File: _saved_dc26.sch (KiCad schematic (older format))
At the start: 60 parts, among them J1 CONN_01X10, J2 CONN_01X10, J3 CONN_01X10

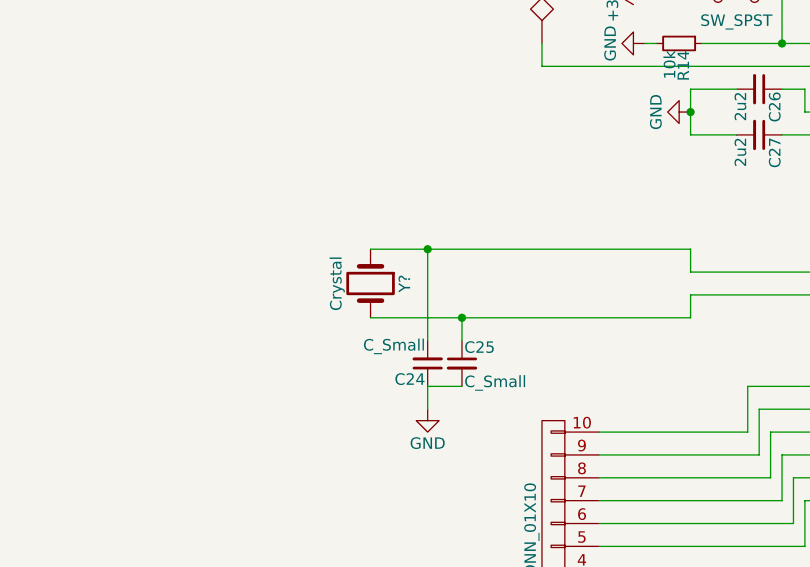
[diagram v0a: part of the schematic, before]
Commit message: zone movement + routing of all circuits
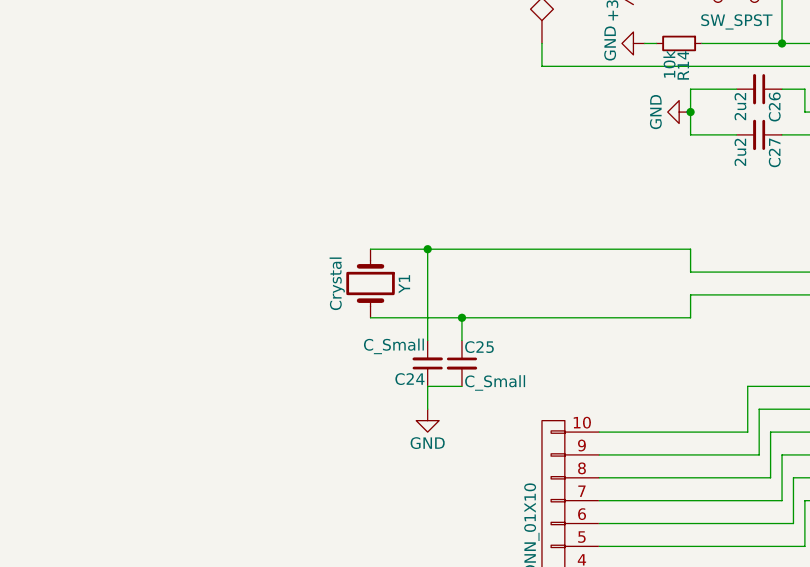
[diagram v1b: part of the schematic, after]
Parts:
- gave numbers to parts that had none: 1
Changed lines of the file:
@@
 $EndComp
 $Comp
-L VCC #PWR01
+L VCC #PWR14
 U 1 1 5AD008FD
 P -5650 -6600
-F 0 "#PWR01" H -5650 -6750 50  0001 C CNN
+F 0 "#PWR14" H -5650 -6750 50  0001 C CNN
 F 1 "VCC" H -5650 -6450 50  0000 C CNN
 F 2 "" H -5650 -6600 50  0001 C CNN
@@
 $EndComp
 $Comp
-L GND #PWR02
+L GND #PWR18
 U 1 1 5AD27FBE
 P -3800 -6700
-F 0 "#PWR02" H -3800 -6950 50  0001 C CNN
+F 0 "#PWR18" H -3800 -6950 50  0001 C CNN
 F 1 "GND" H -3800 -6850 50  0000 C CNN
 F 2 "" H -3800 -6700 50  0001 C CNN
@@
 $EndComp
 $Comp
-L GND #PWR03
+L GND #PWR2
 U 1 1 5AD5BD83
 P -12550 1050
-F 0 "#PWR03" H -12550 800 50  0001 C CNN
+F 0 "#PWR2" H -12550 800 50  0001 C CNN
 F 1 "GND" H -12550 900 50  0000 C CNN
 F 2 "" H -12550 1050 50  0001 C CNN
@@
 $EndComp
 $Comp
-L VCC #PWR04
+L VCC #PWR6
 U 1 1 5AD5C4E4
 P -12300 1050
-F 0 "#PWR04" H -12300 900 50  0001 C CNN
+F 0 "#PWR6" H -12300 900 50  0001 C CNN
 F 1 "VCC" H -12300 1200 50  0000 C CNN
 F 2 "" H -12300 1050 50  0001 C CNN
@@
 $EndComp
 $Comp
-L GND #PWR05
+L GND #PWR20
 U 1 1 5AD6E593
 P -2500 -5100
-F 0 "#PWR05" H -2500 -5350 50  0001 C CNN
+F 0 "#PWR20" H -2500 -5350 50  0001 C CNN
 F 1 "GND" H -2500 -5250 50  0000 C CNN
 F 2 "" H -2500 -5100 50  0001 C CNN
@@
 $EndComp
 $Comp
-L GND #PWR06
+L GND #PWR21
 U 1 1 5AD6F999
 P -2500 -3550
-F 0 "#PWR06" H -2500 -3800 50  0001 C CNN
+F 0 "#PWR21" H -2500 -3800 50  0001 C CNN
 F 1 "GND" H -2500 -3700 50  0000 C CNN
 F 2 "" H -2500 -3550 50  0001 C CNN
@@
 $EndComp
 $Comp
-L GND #PWR07
+L GND #PWR19
 U 1 1 5AD77A72
 P -3600 -800
-F 0 "#PWR07" H -3600 -1050 50  0001 C CNN
+F 0 "#PWR19" H -3600 -1050 50  0001 C CNN
 F 1 "GND" H -3600 -950 50  0000 C CNN
 F 2 "" H -3600 -800 50  0001 C CNN
@@
 $EndComp
 $Comp
-L VCC #PWR08
+L VCC #PWR11
 U 1 1 5AD946E2
 P -7100 12550
-F 0 "#PWR08" H -7100 12400 50  0001 C CNN
+F 0 "#PWR11" H -7100 12400 50  0001 C CNN
 F 1 "VCC" H -7100 12700 50  0000 C CNN
 F 2 "" H -7100 12550 50  0001 C CNN
@@
 $EndComp
 $Comp
-L GND #PWR09
+L GND #PWR10
 U 1 1 5AD98D43
 P -7100 12200
-F 0 "#PWR09" H -7100 11950 50  0001 C CNN
+F 0 "#PWR10" H -7100 11950 50  0001 C CNN
 F 1 "GND" H -7100 12050 50  0000 C CNN
 F 2 "" H -7100 12200 50  0001 C CNN
@@
 $EndComp
 $Comp
-L GND #PWR010
+L GND #PWR17
 U 1 1 5ADAF5CF
 P -3950 10600
-F 0 "#PWR010" H -3950 10350 50  0001 C CNN
+F 0 "#PWR17" H -3950 10350 50  0001 C CNN
 F 1 "GND" H -3950 10450 50  0000 C CNN
 F 2 "" H -3950 10600 50  0001 C CNN
@@
 $EndComp
 $Comp
-L GND #PWR011
+L GND #PWR15
 U 1 1 5ADAFD4C
 P -4000 9500
-F 0 "#PWR011" H -4000 9250 50  0001 C CNN
+F 0 "#PWR15" H -4000 9250 50  0001 C CNN
 F 1 "GND" H -4000 9350 50  0000 C CNN
 F 2 "" H -4000 9500 50  0001 C CNN
@@
 $EndComp
 $Comp
-L GND #PWR012
+L GND #PWR16
 U 1 1 5ADB04C2
 P -4000 12400
-F 0 "#PWR012" H -4000 12150 50  0001 C CNN
+F 0 "#PWR16" H -4000 12150 50  0001 C CNN
 F 1 "GND" H -4000 12250 50  0000 C CNN
 F 2 "" H -4000 12400 50  0001 C CNN
@@
 $EndComp
 $Comp
-L GND #PWR013
+L GND #PWR12
 U 1 1 5B04F2A2
 P -7000 8800
-F 0 "#PWR013" H -7000 8550 50  0001 C CNN
+F 0 "#PWR12" H -7000 8550 50  0001 C CNN
 F 1 "GND" H -7000 8650 50  0000 C CNN
 F 2 "" H -7000 8800 50  0001 C CNN
@@
 $EndComp
 $Comp
-L GND #PWR014
+L GND #PWR1
 U 1 1 5B0E23AB
 P -13400 6550
-F 0 "#PWR014" H -13400 6300 50  0001 C CNN
+F 0 "#PWR1" H -13400 6300 50  0001 C CNN
 F 1 "GND" H -13400 6400 50  0000 C CNN
 F 2 "" H -13400 6550 50  0001 C CNN
@@
 $EndComp
 $Comp
-L +3.3V #PWR016
+L +3.3V #PWR9
 U 1 1 5B0D3E01
 P -7200 2050
-F 0 "#PWR016" H -7200 1900 50  0001 C CNN
+F 0 "#PWR9" H -7200 1900 50  0001 C CNN
 F 1 "+3.3V" H -7200 2190 50  0000 C CNN
 F 2 "" H -7200 2050 50  0001 C CNN
@@
 $EndComp
 $Comp
-L GND #PWR017
+L GND #PWR7
 U 1 1 5B0F137D
 P -12250 5250
-F 0 "#PWR017" H -12250 5000 50  0001 C CNN
+F 0 "#PWR7" H -12250 5000 50  0001 C CNN
 F 1 "GND" H -12250 5100 50  0000 C CNN
 F 2 "" H -12250 5250 50  0001 C CNN
@@
 $EndComp
 $Comp
-L GND #PWR018
+L GND #PWR13
 U 1 1 5B0F6A9C
 P -6200 3750
-F 0 "#PWR018" H -6200 3500 50  0001 C CNN
+F 0 "#PWR13" H -6200 3500 50  0001 C CNN
 F 1 "GND" H -6200 3600 50  0000 C CNN
 F 2 "" H -6200 3750 50  0001 C CNN
@@
 $EndComp
 $Comp
-L +3.3V #PWR019
+L +3.3V #PWR8
 U 1 1 5B11C638
 P -11750 3950
-F 0 "#PWR019" H -11750 3800 50  0001 C CNN
+F 0 "#PWR8" H -11750 3800 50  0001 C CNN
 F 1 "+3.3V" H -11750 4090 50  0000 C CNN
 F 2 "" H -11750 3950 50  0001 C CNN
@@
 $EndComp
 $Comp
-L GND #PWR020
+L GND #PWR5
 U 1 1 5B12677B
 P -12400 4350
-F 0 "#PWR020" H -12400 4100 50  0001 C CNN
+F 0 "#PWR5" H -12400 4100 50  0001 C CNN
 F 1 "GND" H -12400 4200 50  0000 C CNN
 F 2 "" H -12400 4350 50  0001 C CNN
@@
 $EndComp
 $Comp
-L GND #PWR021
+L GND #PWR4
 U 1 1 5B1309D3
 P -12450 4950
-F 0 "#PWR021" H -12450 4700 50  0001 C CNN
+F 0 "#PWR4" H -12450 4700 50  0001 C CNN
 F 1 "GND" H -12450 4800 50  0000 C CNN
 F 2 "" H -12450 4950 50  0001 C CNN
@@
 $EndComp
 $Comp
-L +3.3V #PWR022
+L +3.3V #PWR3
 U 1 1 5B136E3C
 P -12450 4750
-F 0 "#PWR022" H -12450 4600 50  0001 C CNN
+F 0 "#PWR3" H -12450 4600 50  0001 C CNN
 F 1 "+3.3V" H -12450 4890 50  0000 C CNN
 F 2 "" H -12450 4750 50  0001 C CNN
@@
 $EndComp
 $Comp
-L GND #PWR023
+L GND #PWR22
 U 1 1 5B13B631
 P -1800 6650
-F 0 "#PWR023" H -1800 6400 50  0001 C CNN
+F 0 "#PWR22" H -1800 6400 50  0001 C CNN
 F 1 "GND" H -1800 6500 50  0000 C CNN
 F 2 "" H -1800 6650 50  0001 C CNN
@@
 $EndComp
 $Comp
-L GND #PWR024
+L GND #PWR23
 U 1 1 5B1B7467
 P -1200 9050
-F 0 "#PWR024" H -1200 8800 50  0001 C CNN
+F 0 "#PWR23" H -1200 8800 50  0001 C CNN
 F 1 "GND" H -1200 8900 50  0000 C CNN
 F 2 "" H -1200 9050 50  0001 C CNN
@@
 	-13400 6450 -13400 6550
 $Comp
-L Crystal Y?
+L Crystal Y1
 U 1 1 5B113127
 P -13650 6000
-F 0 "Y?" H -13650 6150 50  0000 C CNN
+F 0 "Y1" H -13650 6150 50  0000 C CNN
 F 1 "Crystal" H -13650 5850 50  0000 C CNN
 F 2 "Crystals:Crystal_SMD_5032-2pin_5.0x3.2mm" H -13650 6000 50  0001 C CNN
